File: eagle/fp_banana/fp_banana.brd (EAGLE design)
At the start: 77.6 x 26.6 mm, 9 parts, among them J1 CT3149-0, J2 CT3149-2, J3 CT3149-0, J4 CT3149-2, J5 TSM-105-01-S-SV

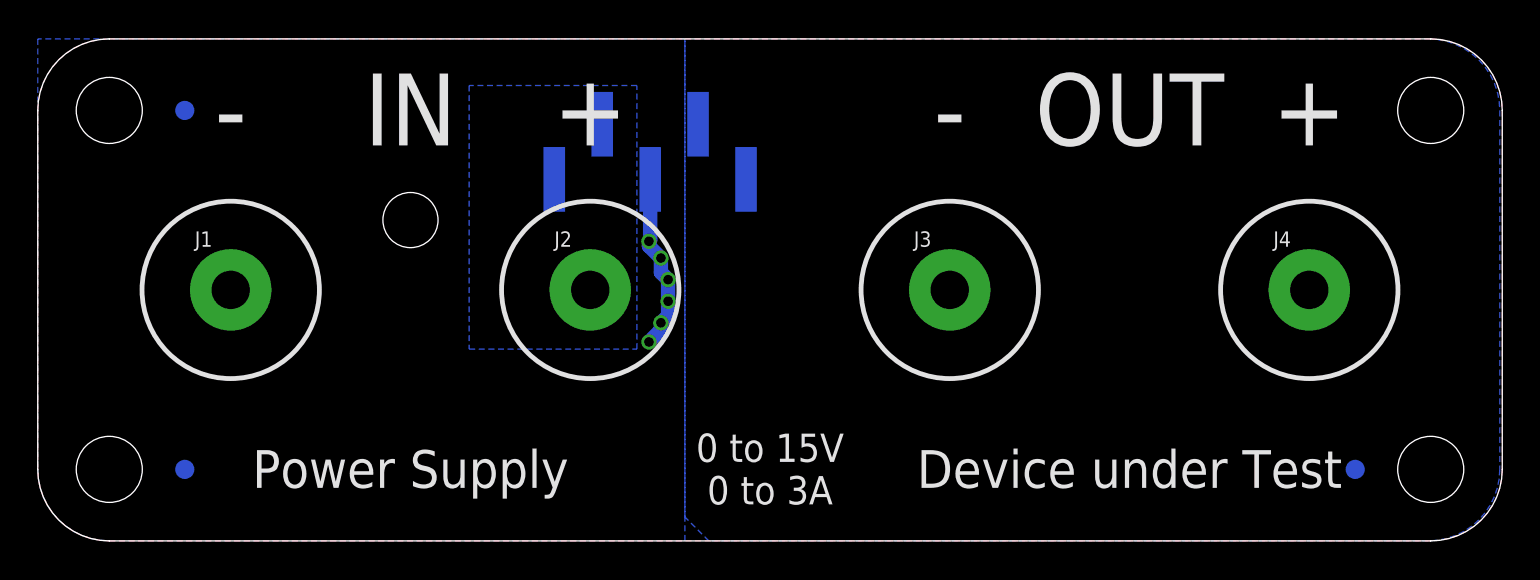
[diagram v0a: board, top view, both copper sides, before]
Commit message: Pre-production update.
* Increased clearances from chassis/enclosure ground.
* Improved text.
* Added gerbers.
* Added USB back panel.
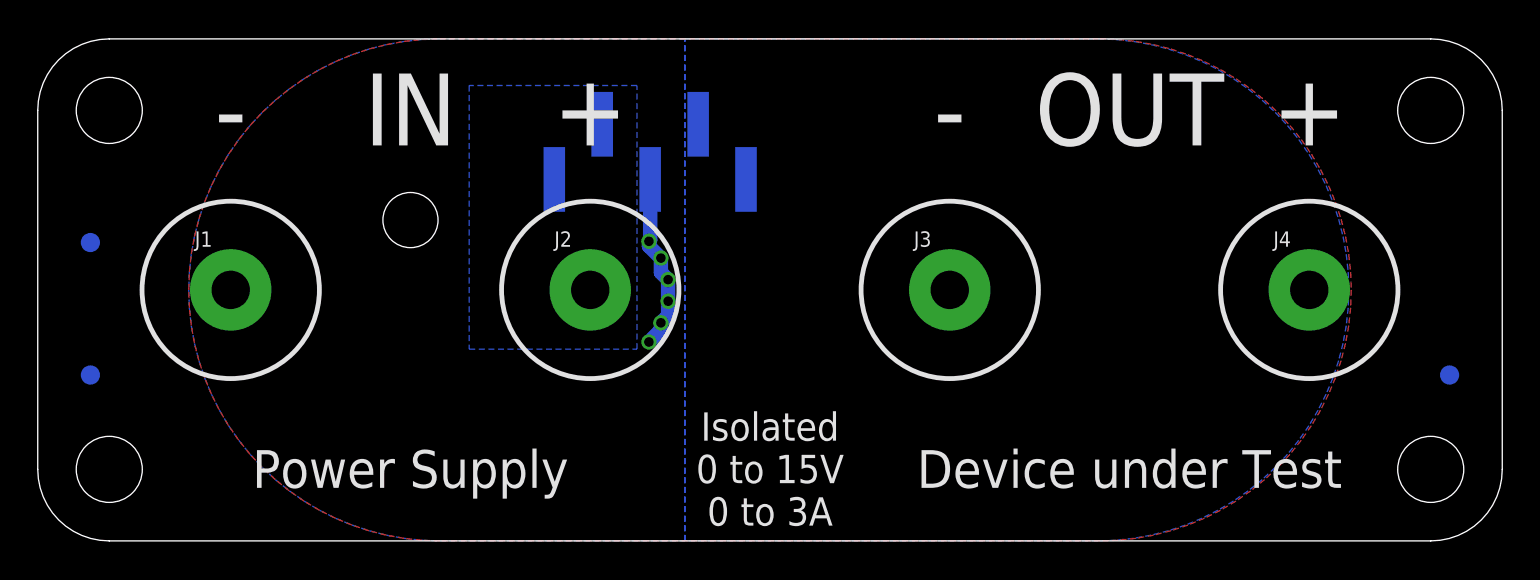
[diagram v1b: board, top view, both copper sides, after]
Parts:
- added H2, H3, H4, H5: HOLE_#6, jetperch:HOLE_3.5MM
- moved FUD3 8.60 mm to (2.79, 15.8)
- moved FUD1 7.07 mm to (2.79, 8.79)
- moved FUD2 7.07 mm to (74.8, 8.79)
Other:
- board text added: "Isolated 0 to 15V 0 to 3A"
- board text added: "Joulescope Front Panel: Banana Jacks rev G 2019 Jetperch LLC"
- board text removed: "0 to 15V 0 to 3A"
- board text removed: "Joulescope Front Panel: Banana Jacks rev D c 2018 Jetperch LLC"
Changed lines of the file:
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@@
 <?xml version="1.0" encoding="utf-8"?>
 <!DOCTYPE eagle SYSTEM "eagle.dtd">
-<eagle version="9.2.2">
+<eagle version="9.3.2">
 <drawing>
 <settings>
@@
 <setting verticaltext="up"/>
 </settings>
-<grid distance="0.05" unitdist="inch" unit="mil" style="lines" multiple="1" display="no" altdistance="0.005" altunitdist="inch" altunit="inch"/>
+<grid distance="1" unitdist="mm" unit="mm" style="lines" multiple="1" display="no" altdistance="0.005" altunitdist="inch" altunit="inch"/>
 <layers>
 <layer number="1" name="Top" color="4" fill="1" visible="yes" active="yes"/>
@@
 <layer number="118" name="Rect_Pads" color="7" fill="1" visible="yes" active="yes"/>
 <layer number="121" name="_tsilk" color="7" fill="1" visible="yes" active="yes"/>
-<layer number="122" name="_bsilk" color="7" fill="1" visible="yes" active="yes"/>
+<layer number="122" name="_bsilk" color="7" fill="1" visible="no" active="yes"/>
 <layer number="123" name="tTestmark" color="7" fill="1" visible="yes" active="yes"/>
 <layer number="124" name="bTestmark" color="7" fill="1" visible="yes" active="yes"/>
@@
 <wire x1="73.81" y1="26.6" x2="3.79" y2="26.6" width="0" layer="20"/>
 <wire x1="3.79" y1="26.6" x2="0" y2="22.81" width="0" layer="20" curve="90"/>
-<hole x="3.79" y="3.79" drill="3.5"/>
-<hole x="73.81" y="3.79" drill="3.5"/>
-<hole x="3.79" y="22.81" drill="3.5"/>
-<hole x="73.81" y="22.81" drill="3.5"/>
 <text x="10.225" y="22.86" size="3.81" layer="121" font="vector" ratio="20" align="center">-</text>
 <text x="29.275" y="22.86" size="3.81" layer="121" font="vector" ratio="20" align="center">+</text>
@@
 <text x="19.75" y="22.86" size="3.81" layer="121" font="vector" ratio="20" align="center">IN</text>
 <text x="57.85" y="22.86" size="3.81" layer="121" font="vector" ratio="20" align="center">OUT</text>
-<text x="38.8" y="3.81" size="1.27" layer="122" font="vector" ratio="20" rot="MR0" align="center">Joulescope Front Panel: Banana Jacks rev D
- c  2018 Jetperch LLC</text>
-<circle x="46.99" y="2.667" radius="1.016" width="0.254" layer="122"/>
+<text x="38.8" y="3.81" size="1.27" layer="122" font="vector" ratio="20" rot="MR0" align="center">Joulescope Front Panel: Banana Jacks rev G
+2019 Jetperch LLC</text>
 <dimension x1="0" y1="22.81" x2="77.6" y2="19.05" x3="38.8" y3="40.64" textsize="1.778" layer="47" dtype="horizontal"/>
 <dimension x1="3.79" y1="0" x2="7.62" y2="26.6" x3="-6.35" y3="13.3" textsize="1.778" layer="47" dtype="vertical"/>
@@
 <text x="19.75" y="3.81" size="2" layer="121" font="vector" ratio="20" align="center">Power Supply</text>
 <text x="57.85" y="3.81" size="2" layer="121" font="vector" ratio="20" align="center">Device under Test</text>
-<text x="38.8" y="3.81" size="1.5" layer="121" font="vector" ratio="20" align="center">0 to 15V
+<text x="38.8" y="3.81" size="1.5" layer="121" font="vector" ratio="20" align="center">Isolated
+0 to 15V
 0 to 3A</text>
 <wire x1="0" y1="17.3" x2="16.64" y2="17.3" width="0.254" layer="22"/>
@@
 <attribute name="POPULATE" value="1" x="19.75" y="17" size="1.778" layer="27" display="off"/>
 </element>
-<element name="FUD1" library="jetperch" package="FIDUCIAL_1MM_2MM" value="FIDUCIAL_1MM" x="7.79" y="3.79" smashed="yes" rot="MR0">
-<attribute name="POPULATE" value="0" x="7.79" y="3.79" size="1.778" layer="28" rot="MR0" display="off"/>
-</element>
-<element name="FUD2" library="jetperch" package="FIDUCIAL_1MM_2MM" value="FIDUCIAL_1MM" x="69.81" y="3.79" smashed="yes" rot="MR0">
-<attribute name="POPULATE" value="0" x="69.81" y="3.79" size="1.778" layer="28" rot="MR0" display="off"/>
-</element>
-<element name="FUD3" library="jetperch" package="FIDUCIAL_1MM_2MM" value="FIDUCIAL_1MM" x="7.79" y="22.81" smashed="yes" rot="MR0">
-<attribute name="POPULATE" value="0" x="7.79" y="22.81" size="1.778" layer="28" rot="MR0" display="off"/>
-</element>
+<element name="FUD1" library="jetperch" package="FIDUCIAL_1MM_2MM" value="FIDUCIAL_1MM" x="2.79" y="8.79" smashed="yes" rot="MR0">
+<attribute name="POPULATE" value="0" x="2.79" y="8.79" size="1.778" layer="28" rot="MR0" display="off"/>
+</element>
+<element name="FUD2" library="jetperch" package="FIDUCIAL_1MM_2MM" value="FIDUCIAL_1MM" x="74.81" y="8.79" smashed="yes" rot="MR0">
+<attribute name="POPULATE" value="0" x="74.81" y="8.79" size="1.778" layer="28" rot="MR0" display="off"/>
+</element>
+<element name="FUD3" library="jetperch" package="FIDUCIAL_1MM_2MM" value="FIDUCIAL_1MM" x="2.79" y="15.81" smashed="yes" rot="MR0">
+<attribute name="POPULATE" value="0" x="2.79" y="15.81" size="1.778" layer="28" rot="MR0" display="off"/>
+</element>
+<element name="H2" library="jetperch" package="HOLE_3.5MM" value="HOLE_#6" x="3.79" y="3.79" smashed="yes"/>
+<element name="H3" library="jetperch" package="HOLE_3.5MM" value="HOLE_#6" x="73.81" y="22.81" smashed="yes"/>
+<element name="H4" library="jetperch" package="HOLE_3.5MM" value="HOLE_#6" x="3.79" y="22.81" smashed="yes"/>
+<element name="H5" library="jetperch" package="HOLE_3.5MM" value="HOLE_#6" x="73.81" y="3.79" smashed="yes"/>
 </elements>
 <signals>
@@
 <contactref element="J1" pad="A"/>
 <contactref element="J3" pad="A"/>
-<polygon width="0.1524" layer="1" thermals="no">
-<vertex x="73.81" y="0"/>
-<vertex x="3.79" y="0" curve="-90"/>
-<vertex x="0" y="3.79"/>
-<vertex x="0" y="22.81" curve="-90"/>
-<vertex x="3.79" y="26.6"/>
-<vertex x="73.81" y="26.6" curve="-90"/>
-<vertex x="77.6" y="22.81"/>
-<vertex x="77.6" y="3.79" curve="-90"/>
+<polygon width="0.254" layer="1" thermals="no">
+<vertex x="21.3" y="26.6"/>
+<vertex x="56.3" y="26.6" curve="-90"/>
+<vertex x="69.6" y="13.3" curve="-90"/>
+<vertex x="56.3" y="0"/>
+<vertex x="21.3" y="0" curve="-90"/>
+<vertex x="8" y="13.3" curve="-90"/>
 </polygon>
 <wire x1="32.45" y1="19.1545" x2="32.45" y2="15.94" width="0.762" layer="16"/>
@@
 <via x="33.02" y="11.557" extent="1-16" drill="0.508"/>
 <polygon width="0.254" layer="16" thermals="no" rank="3">
-<vertex x="0" y="26.6"/>
-<vertex x="0" y="3.79" curve="90"/>
-<vertex x="3.79" y="0"/>
+<vertex x="34.29" y="26.6"/>
+<vertex x="21.3" y="26.6" curve="90"/>
+<vertex x="8" y="13.3" curve="90"/>
+<vertex x="21.3" y="0"/>
 <vertex x="34.29" y="0"/>
-<vertex x="34.29" y="26.6"/>
 </polygon>
 <via x="32.385" y="10.541" extent="1-16" drill="0.508"/>
@@
 <polygon width="0.254" layer="16" isolate="0.254" thermals="no">
 <vertex x="34.29" y="26.6"/>
-<vertex x="39.37" y="26.6"/>
-<vertex x="73.68" y="26.6" curve="-90"/>
-<vertex x="77.47" y="22.81"/>
-<vertex x="77.47" y="3.79" curve="-90"/>
-<vertex x="73.68" y="0"/>
-<vertex x="35.56" y="0"/>
-<vertex x="34.29" y="1.27"/>
-<vertex x="34.29" y="19.05"/>
+<vertex x="56.17" y="26.6" curve="-90"/>
+<vertex x="69.47" y="13.3" curve="-90"/>
+<vertex x="56.17" y="0"/>
+<vertex x="34.29" y="0"/>
 </polygon>
 </signal>

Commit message: Banana Jack front panel rev H
* Increased 5x1 connector pad width from 45 mil to 50 mil.
* Added brief fab notes & fab drawing.
* Improved dimensioning for clarity.
* Removed excessive number of EXT_NEG vias.
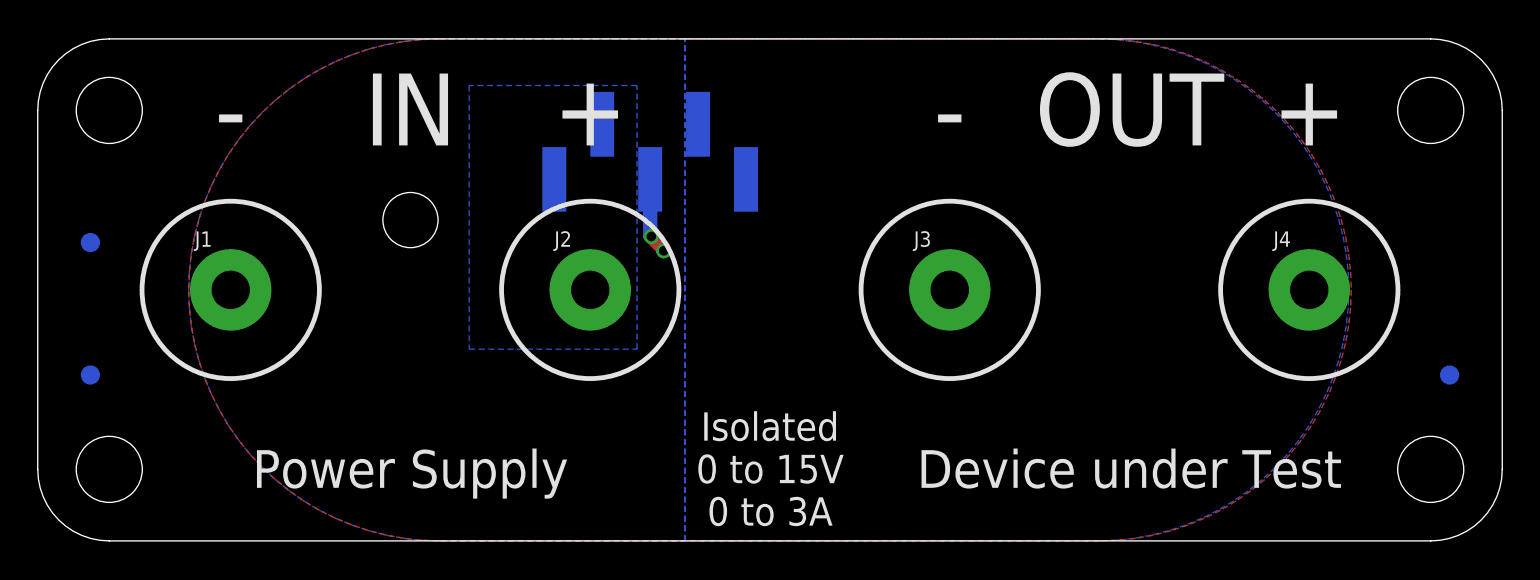
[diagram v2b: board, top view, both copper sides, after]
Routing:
- net EXT_NEG: track 9.48 -> 4.08 mm, vias 6 -> 2
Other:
- board text added: "All dimensions in millimeters Place all markings on back (including pcb order number). Add flammability rating marking on back, such as 94V-0. The front-side surface is cosmetic - reject units with scratches and blemishes."
- board text added: "Joulescope Front Panel: Banana Jacks rev H 2019 Jetperch LLC"
- board text removed: "All dimensions in millimeters"
- board text removed: "Joulescope Front Panel: Banana Jacks rev G 2019 Jetperch LLC"
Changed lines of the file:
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@@
 <?xml version="1.0" encoding="utf-8"?>
 <!DOCTYPE eagle SYSTEM "eagle.dtd">
-<eagle version="9.3.2">
+<eagle version="9.5.0">
 <drawing>
 <settings>
@@
 <setting verticaltext="up"/>
 </settings>
-<grid distance="1" unitdist="mm" unit="mm" style="lines" multiple="1" display="no" altdistance="0.005" altunitdist="inch" altunit="inch"/>
+<grid distance="0.1" unitdist="inch" unit="inch" style="lines" multiple="1" display="no" altdistance="0.005" altunitdist="inch" altunit="inch"/>
 <layers>
 <layer number="1" name="Top" color="4" fill="1" visible="yes" active="yes"/>
@@
 <layer number="118" name="Rect_Pads" color="7" fill="1" visible="yes" active="yes"/>
 <layer number="121" name="_tsilk" color="7" fill="1" visible="yes" active="yes"/>
-<layer number="122" name="_bsilk" color="7" fill="1" visible="no" active="yes"/>
+<layer number="122" name="_bsilk" color="7" fill="1" visible="yes" active="yes"/>
 <layer number="123" name="tTestmark" color="7" fill="1" visible="yes" active="yes"/>
 <layer number="124" name="bTestmark" color="7" fill="1" visible="yes" active="yes"/>
@@
 <text x="19.75" y="22.86" size="3.81" layer="121" font="vector" ratio="20" align="center">IN</text>
 <text x="57.85" y="22.86" size="3.81" layer="121" font="vector" ratio="20" align="center">OUT</text>
-<text x="38.8" y="3.81" size="1.27" layer="122" font="vector" ratio="20" rot="MR0" align="center">Joulescope Front Panel: Banana Jacks rev G
+<text x="38.8" y="3.81" size="1.27" layer="122" font="vector" ratio="20" rot="MR0" align="center">Joulescope Front Panel: Banana Jacks rev H
 2019 Jetperch LLC</text>
 <dimension x1="0" y1="22.81" x2="77.6" y2="19.05" x3="38.8" y3="40.64" textsize="1.778" layer="47" dtype="horizontal"/>
-<dimension x1="3.79" y1="0" x2="7.62" y2="26.6" x3="-6.35" y3="13.3" textsize="1.778" layer="47" dtype="vertical"/>
+<dimension x1="3.79" y1="0" x2="3.79" y2="26.6" x3="-9.35" y3="13.3" textsize="1.778" layer="47" dtype="vertical"/>
 <dimension x1="0" y1="3.79" x2="3.79" y2="3.79" x3="1.895" y3="-8.89" textsize="1.778" layer="47" dtype="horizontal"/>
 <dimension x1="3.79" y1="0" x2="3.79" y2="3.79" x3="-2.54" y3="1.895" textsize="1.778" layer="47" dtype="vertical"/>
 <dimension x1="2.5483125" y1="21.576828125" x2="5.0316875" y2="24.043171875" x3="-6.349990625" y3="33.0200125" textsize="1.778" layer="47" dtype="diameter"/>
 <dimension x1="73.81" y1="3.79" x2="76.74625" y2="1.393640625" x3="82.78919375" y3="-3.53818125" textsize="1.778" layer="47" dtype="radius"/>
-<dimension x1="38.8" y1="20.615" x2="39.37" y2="26.67" x3="82.55" y3="23.6425" textsize="1.778" layer="47" dtype="vertical"/>
+<dimension x1="32.45" y1="20.615" x2="77.6" y2="26.67" x3="82.55" y3="23.6425" textsize="1.778" layer="47" dtype="vertical"/>
 <dimension x1="10.225" y1="13.3" x2="29.275" y2="13.3" x3="19.75" y3="-3.81" textsize="1.778" layer="47" dtype="horizontal"/>
-<dimension x1="48.325" y1="13.3" x2="67.375" y2="12.7" x3="57.85" y3="-3.81" textsize="1.778" layer="47" dtype="horizontal"/>
-<dimension x1="29.275" y1="13.3" x2="48.325" y2="11.43" x3="38.8" y3="-3.81" textsize="1.778" layer="47" dtype="horizontal"/>
+<dimension x1="48.325" y1="13.3" x2="67.375" y2="13.3" x3="57.85" y3="-3.81" textsize="1.778" layer="47" dtype="horizontal"/>
+<dimension x1="29.275" y1="13.3" x2="48.325" y2="13.3" x3="38.8" y3="-3.81" textsize="1.778" layer="47" dtype="horizontal"/>
 <rectangle x1="0" y1="17.3" x2="25.5" y2="19.3" layer="40"/>
 <rectangle x1="52.1" y1="17.3" x2="77.6" y2="19.3" layer="40"/>
@@
 <wire x1="39.37" y1="18.3" x2="77.6" y2="18.3" width="0.127" layer="22" style="shortdash"/>
 <dimension x1="77.6" y1="0" x2="77.6" y2="18.3" x3="93.63" y3="9.15" textsize="1.778" layer="47"/>
-<dimension x1="77.6" y1="0" x2="77.6" y2="13.3" x3="87.4214875" y3="6.65" textsize="1.778" layer="47"/>
-<dimension x1="0" y1="26.6" x2="32.45" y2="26.6" x3="16.225" y3="32.984990625" textsize="1.778" layer="47"/>
-<dimension x1="38.8" y1="26.6" x2="19.75" y2="26.6" x3="29.275" y3="29.21" textsize="1.778" layer="47"/>
+<dimension x1="77.6" y1="0" x2="67.375" y2="13.3" x3="87.4214875" y3="6.65" textsize="1.778" layer="47" dtype="vertical"/>
+<dimension x1="0" y1="26.6" x2="32.45" y2="20.615" x3="16.225" y3="32.984990625" textsize="1.778" layer="47" dtype="horizontal"/>
+<dimension x1="38.8" y1="26.6" x2="19.75" y2="17" x3="29.275" y3="28.709315625" textsize="1.778" layer="47" dtype="horizontal"/>
 <dimension x1="0" y1="26.6" x2="38.8" y2="26.6" x3="19.4" y3="36.794990625" textsize="1.778" layer="47"/>
-<text x="43.18" y="-10.16" size="1.778" layer="153">All dimensions in millimeters</text>
+<text x="0.18" y="-24.16" size="1.778" layer="153">All dimensions in millimeters
+Place all markings on back (including pcb order number).
+Add flammability rating marking on back, such as 94V-0.
+The front-side surface is cosmetic - reject units with scratches and blemishes.</text>
 <wire x1="0" y1="19.3" x2="25.53" y2="19.3" width="0.254" layer="22"/>
 <wire x1="0" y1="18.3" x2="16.64" y2="18.3" width="0.127" layer="22" style="shortdash"/>
 <wire x1="39.37" y1="17.3" x2="77.6" y2="17.3" width="0.254" layer="22"/>
+<dimension x1="19.75" y1="17" x2="3.79" y2="26.6" x3="-4.35" y3="21.8" textsize="1.778" layer="47" dtype="vertical"/>
 </plain>
 <attributes>
@@
 <vertex x="8" y="13.3" curve="-90"/>
 </polygon>
-<wire x1="32.45" y1="19.1545" x2="32.45" y2="15.94" width="0.762" layer="16"/>
-<wire x1="32.45" y1="15.94" x2="32.385" y2="15.875" width="0.762" layer="16"/>
-<via x="32.385" y="15.875" extent="1-16" drill="0.508"/>
-<via x="33.02" y="14.986" extent="1-16" drill="0.508"/>
-<via x="33.401" y="13.843" extent="1-16" drill="0.508"/>
-<via x="33.401" y="12.7" extent="1-16" drill="0.508"/>
-<via x="33.02" y="11.557" extent="1-16" drill="0.508"/>
+<wire x1="32.45" y1="19.1545" x2="32.45" y2="16.191" width="0.762" layer="16"/>
+<wire x1="32.45" y1="16.191" x2="32.512" y2="16.129" width="0.762" layer="16"/>
+<via x="32.512" y="16.129" extent="1-16" drill="0.508"/>
 <polygon width="0.254" layer="16" thermals="no" rank="3">
 <vertex x="34.29" y="26.6"/>
@@
 <vertex x="34.29" y="0"/>
 </polygon>
-<via x="32.385" y="10.541" extent="1-16" drill="0.508"/>
-<wire x1="32.385" y1="15.875" x2="32.385" y2="15.621" width="0.76" layer="16"/>
-<wire x1="32.385" y1="15.621" x2="33.02" y2="14.986" width="0.76" layer="16"/>
-<wire x1="33.02" y1="14.986" x2="33.02" y2="14.224" width="0.76" layer="16"/>
-<wire x1="33.02" y1="14.224" x2="33.401" y2="13.843" width="0.76" layer="16"/>
-<wire x1="33.401" y1="13.843" x2="33.401" y2="12.7" width="0.76" layer="16"/>
-<wire x1="33.401" y1="12.7" x2="33.401" y2="11.938" width="0.76" layer="16"/>
-<wire x1="33.401" y1="11.938" x2="33.02" y2="11.557" width="0.76" layer="16"/>
-<wire x1="33.02" y1="11.557" x2="33.02" y2="11.176" width="0.76" layer="16"/>
-<wire x1="33.02" y1="11.176" x2="32.385" y2="10.541" width="0.76" layer="16"/>
+<via x="33.167" y="15.369" extent="1-16" drill="0.508"/>
+<wire x1="32.512" y1="16.129" x2="33.167" y2="15.474" width="0.762" layer="1"/>
+<wire x1="33.167" y1="15.474" x2="33.167" y2="15.369" width="0.762" layer="1"/>
 </signal>
 <signal name="EXT_OUT">
